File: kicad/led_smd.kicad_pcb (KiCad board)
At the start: 2 copper layers, 10.2 x 38.1 mm, 8 parts, among them J1 INPUT, J2 OUTPUT, J3 USB_OTG, Q1 SI2306, SW1 SW DOWN, SW2 SW UP, U1 PIC10F200-IP

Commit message: Schematic + PCB SMD WiP
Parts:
- added C1: 100nF, Capacitors_SMD:C_0402, F.Cu at (136.7, 96.0)
- R1: footprint Resistors_SMD:R_0201 -> Resistors_SMD:R_0402
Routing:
- net GNDD: track 46.1 -> 53.8 mm, vias 1 -> 2
- net (no net): track 2.54 -> 0.00 mm
- added copper zone on B.Cu, net GNDD
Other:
- net class power added: clearance 0.2, trace_width 1.27, via_dia 0.6, via_drill 0.4

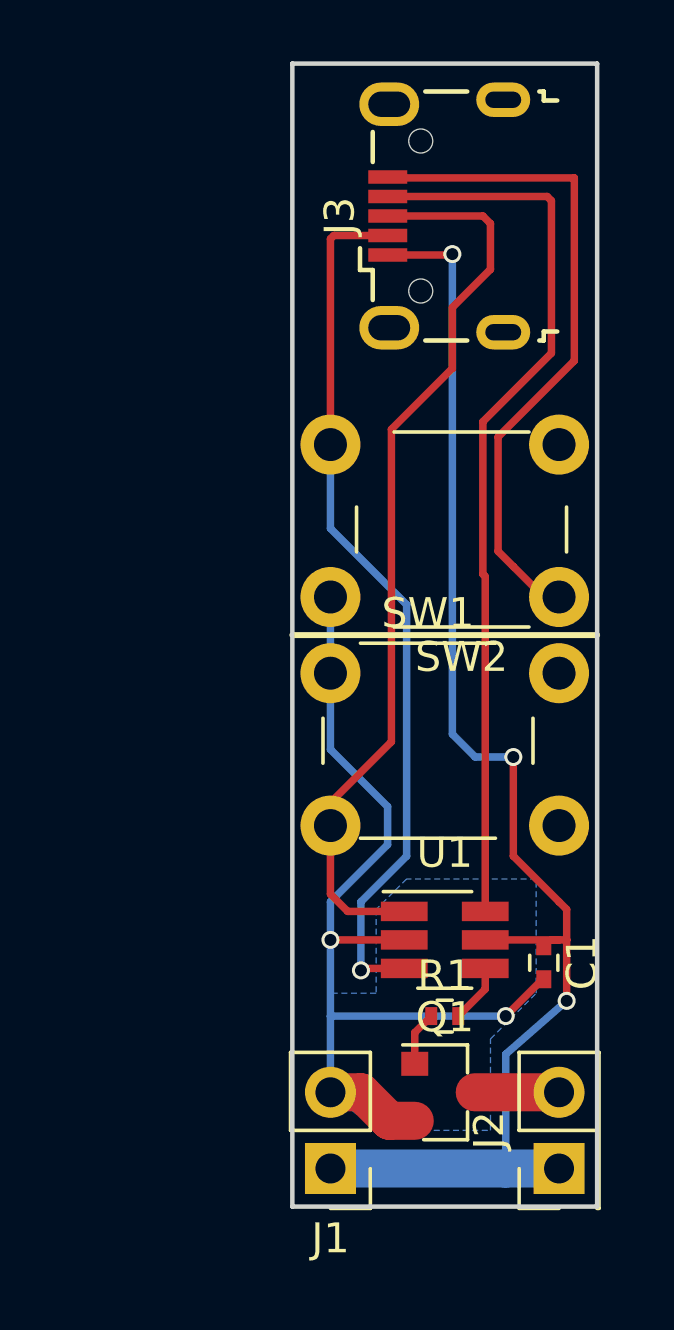
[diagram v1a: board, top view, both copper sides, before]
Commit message: Schematic + PCB SMD new version
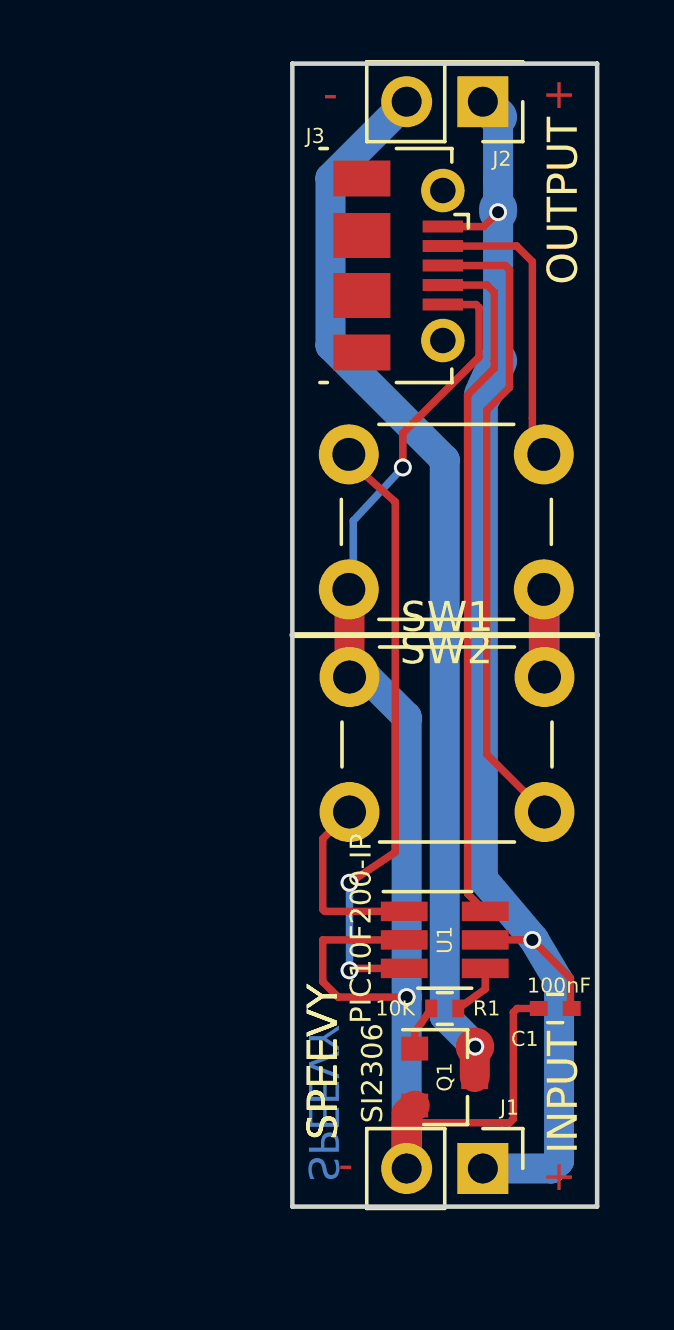
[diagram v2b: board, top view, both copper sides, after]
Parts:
- J3: footprint Connectors_USB:USB_Micro-B_Wuerth-629105150521 -> Connectors_USB:USB_Micro-B_Molex-105017-0001
- moved J2 35.7 mm to (134.6, 67.3), turned to 180 degrees
- moved J1 5.08 mm to (134.6, 102.9), turned to 270 degrees
- moved J3 2.92 mm to (130.9, 72.8), turned to 270 degrees
- moved C1 1.57 mm to (137.0, 97.5), turned to 180 degrees
- moved SW1 0.65 mm to (130.2, 86.5)
- moved SW2 0.57 mm to (136.7, 83.6)
- moved Q1 0.51 mm to (133.3, 99.8)
- moved R1 0.25 mm to (133.3, 97.5)
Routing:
- net Net-(J2-Pad2): track 2.81 -> 35.6 mm, vias 0 -> 1
- net Net-(J3-Pad4): track 30.2 -> 23.1 mm
- net Net-(J3-Pad3): track 30.8 -> 27.8 mm
- net GNDD: track 53.8 -> 56.5 mm
- net Net-(J3-Pad2): track 29.5 -> 30.9 mm, vias 1 -> 2
- net VDD: track 46.5 -> 45.6 mm, vias 3 -> 2
- removed copper zone on B.Cu, net GNDD
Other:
- board text added: "+"
- board text added: "-"
- board text added: "INPUT"
- board text added: "OUTPUT"
- board text added: "SPEEVY"
